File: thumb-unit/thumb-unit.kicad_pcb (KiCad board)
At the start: 2 copper layers, 82.5 x 79 mm, 24 parts, among them J1 Conn_01x10, SW1 SW_SPDT, SW2 SW_Push, SW3 SW_Push, SW4 SW_Push, SW5 SW_Push, U1 xiao-ble, U2 PMW3610, U3 TLV70218_SOT23-5

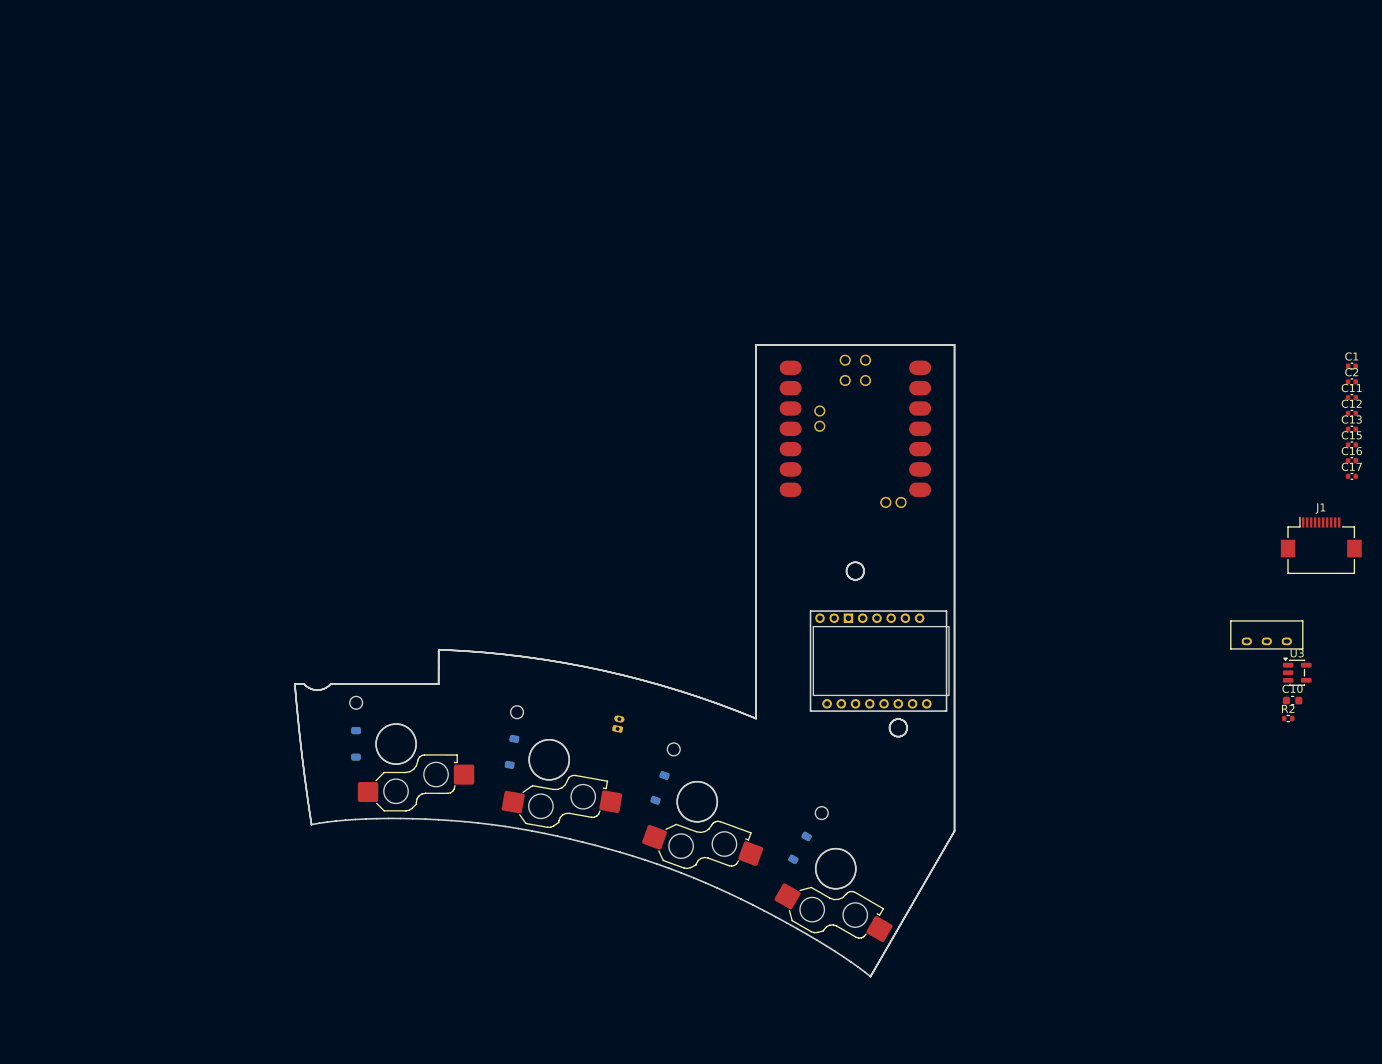
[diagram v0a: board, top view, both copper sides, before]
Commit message: feat: 親指ユニットのpcb設計
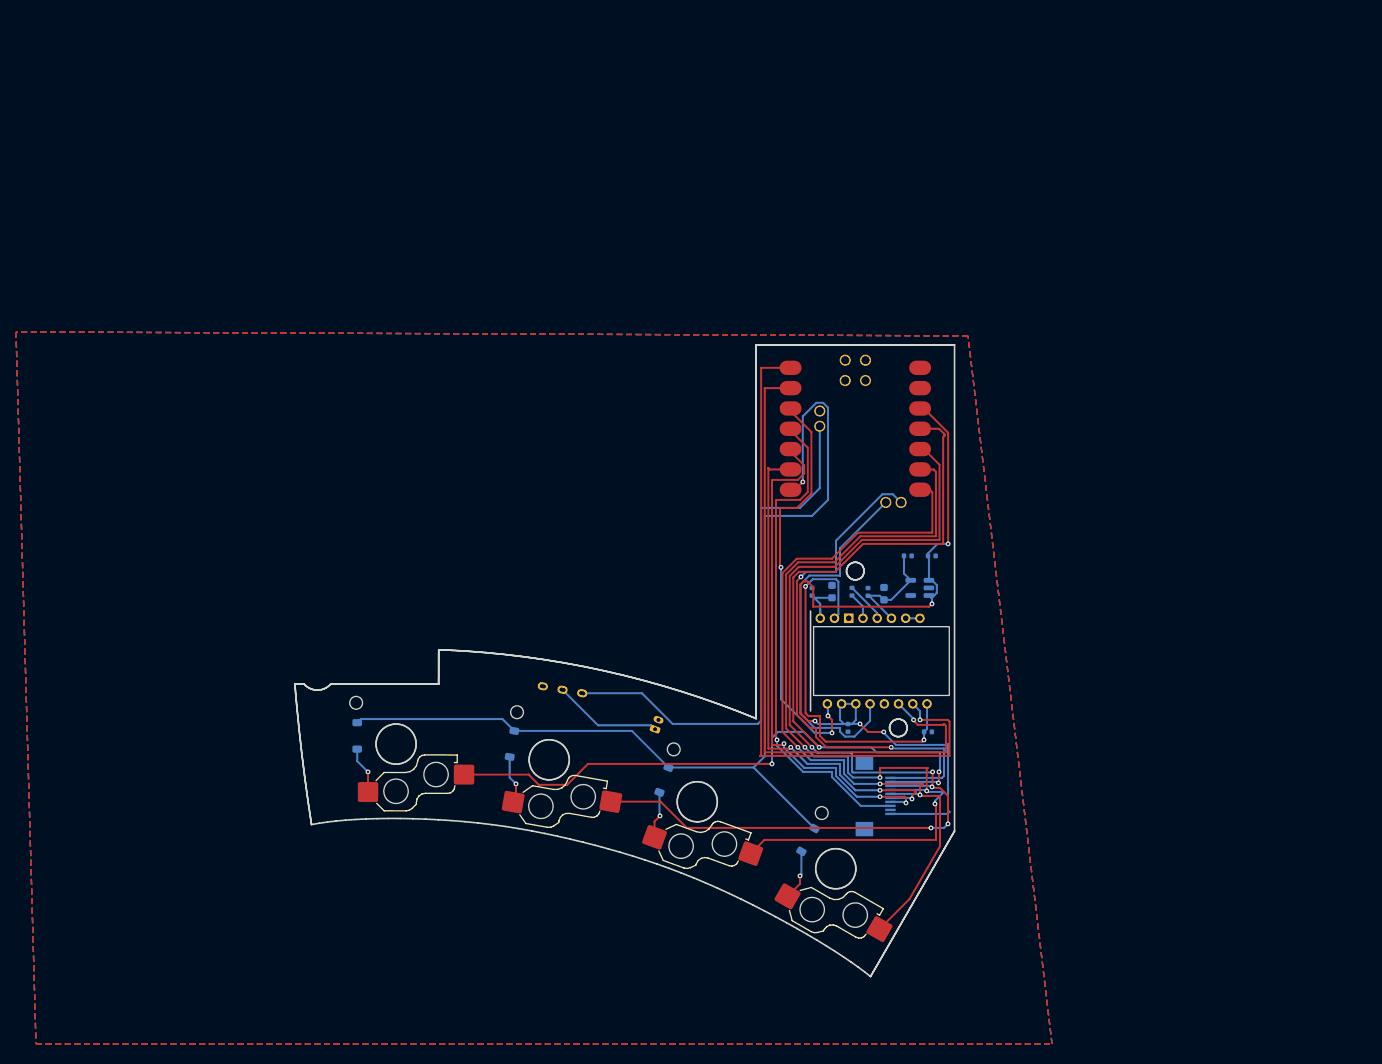
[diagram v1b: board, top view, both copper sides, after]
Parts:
- removed R2: 10k, Resistor_SMD:R_0402_1005Metric
- C1, C12, C15, C16, C2, J1, SW1, U3: moved to B.Cu
- C10: value 10uF -> 10uF X7R; moved to B.Cu
- C11: value 10nF -> 10nF X7R; moved to B.Cu
- C13: value 100nF -> 100nF X7R; moved to B.Cu
- C17: value 3.3uF -> 3.3uF/16V; footprint Capacitor_SMD:C_0402_1005Metric -> Capacitor_SMD:C_0603_1608Metric; moved to B.Cu
- moved SW1 88.1 mm to (106.0, 141.7), turned to 170 degrees
- moved C15 72.2 mm to (141.5, 147.5), turned to 90 degrees
- moved C11 71.7 mm to (137.0, 130.5), turned to -90 degrees
- moved C12 66.3 mm to (151.5, 148.0)
- moved C13 65.7 mm to (142.0, 130.5), turned to -90 degrees
- moved J1 64.4 mm to (144.9, 156.0), turned to 90 degrees
- moved C16 62.7 mm to (144.0, 130.5), turned to 90 degrees
- moved C17 60.3 mm to (146.0, 130.7), turned to 90 degrees
- moved C2 59.6 mm to (149.0, 126.0), turned to 180 degrees
- moved C10 59.2 mm to (139.5, 130.5), turned to -90 degrees
- moved C1 57.6 mm to (152.0, 126.0), turned to 180 degrees
- moved U3 48.3 mm to (150.5, 130.0), turned to 180 degrees
- moved BT1 4.68 mm to (117.4, 147.7), turned to 70 degrees
- moved D1 1.41 mm to (136.5, 161.5), turned to 60 degrees
- moved D2 1.12 mm to (118.5, 154.0), turned to 70 degrees
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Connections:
- C10 pad 1: Net-(U2-VCP) -> GND
- C10 pad 2: GND -> Net-(U2-VCP)
- C11 pad 1: Net-(U2-VCP) -> GND
- C11 pad 2: GND -> Net-(U2-VCP)
- C12 pad 1: +1V8 -> Net-(U2-+VCSEL)
- C12 pad 2: +1V8 -> GND
- C16 pad 1: GND -> +1V8
- C16 pad 2: +1V8 -> GND
- C17 pad 1: GND -> +1V8
- C17 pad 2: +1V8 -> GND
- U2 pad 1: +1V8 -> Net-(U2-+VCSEL)
- U2 pad 10: +1V8 -> Net-(U2-+VCSEL)
- U2 pad 15: +1V8 -> Net-(U2--VCSEL)
- U2 pad 16: +1V8 -> Net-(U2--VCSEL)
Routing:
- net /COL3: track 0.00 -> 135.4 mm, vias 0 -> 4
- net /COL2: track 0.00 -> 130.1 mm, vias 0 -> 5
- net /ROW3: track 0.00 -> 130.0 mm, vias 0 -> 1
- net /COL1: track 0.00 -> 112.4 mm, vias 0 -> 4
- net +3V3: track 0.00 -> 109.3 mm, vias 0 -> 5
- net /COL0: track 0.00 -> 95.3 mm, vias 0 -> 3
- net /SDIO: track 0.00 -> 85.9 mm, vias 0 -> 1
- net /SCLK: track 0.00 -> 81.6 mm, vias 0 -> 1
- net /COL4: track 0.00 -> 68.0 mm, vias 0 -> 2
- net /BAT_SW: track 0.00 -> 66.8 mm
- net /ROW1: track 0.00 -> 64.7 mm, vias 0 -> 3
- net /ROW2: track 0.00 -> 63.0 mm, vias 0 -> 3
- net /ROW0: track 0.00 -> 62.0 mm, vias 0 -> 1
- net /MOTION: track 0.00 -> 52.6 mm, vias 0 -> 3
- net Net-(U2-+VCSEL): track 0.00 -> 47.8 mm, vias 0 -> 2
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- added copper zone on B.Cu, net GND
- added copper zone on F.Cu, net GND
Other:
- outline, holes or cut-outs redrawn

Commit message: feat: 親指ユニットのpcb設計
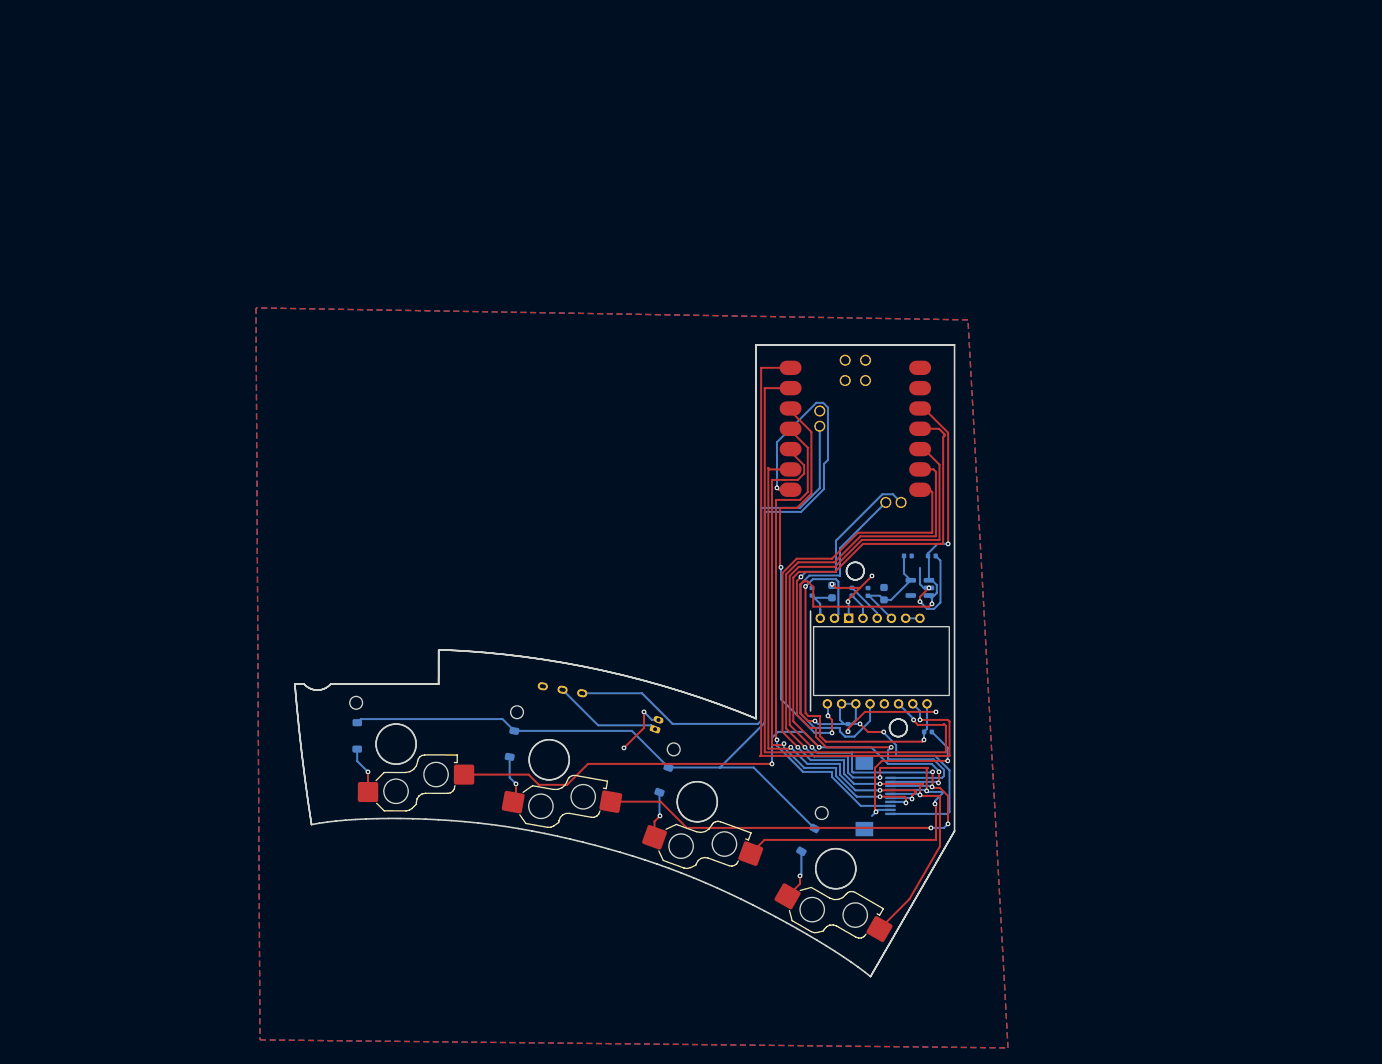
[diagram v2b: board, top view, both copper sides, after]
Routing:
- net GND: track 0.00 -> 67.4 mm, vias 0 -> 11
- net /ROW3: track 130.0 -> 132.0 mm
- net /COL3: track 135.4 -> 134.0 mm
- net +3V3: track 109.3 -> 108.1 mm

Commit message: feat: 親指dxfファイルをインポートして調整した
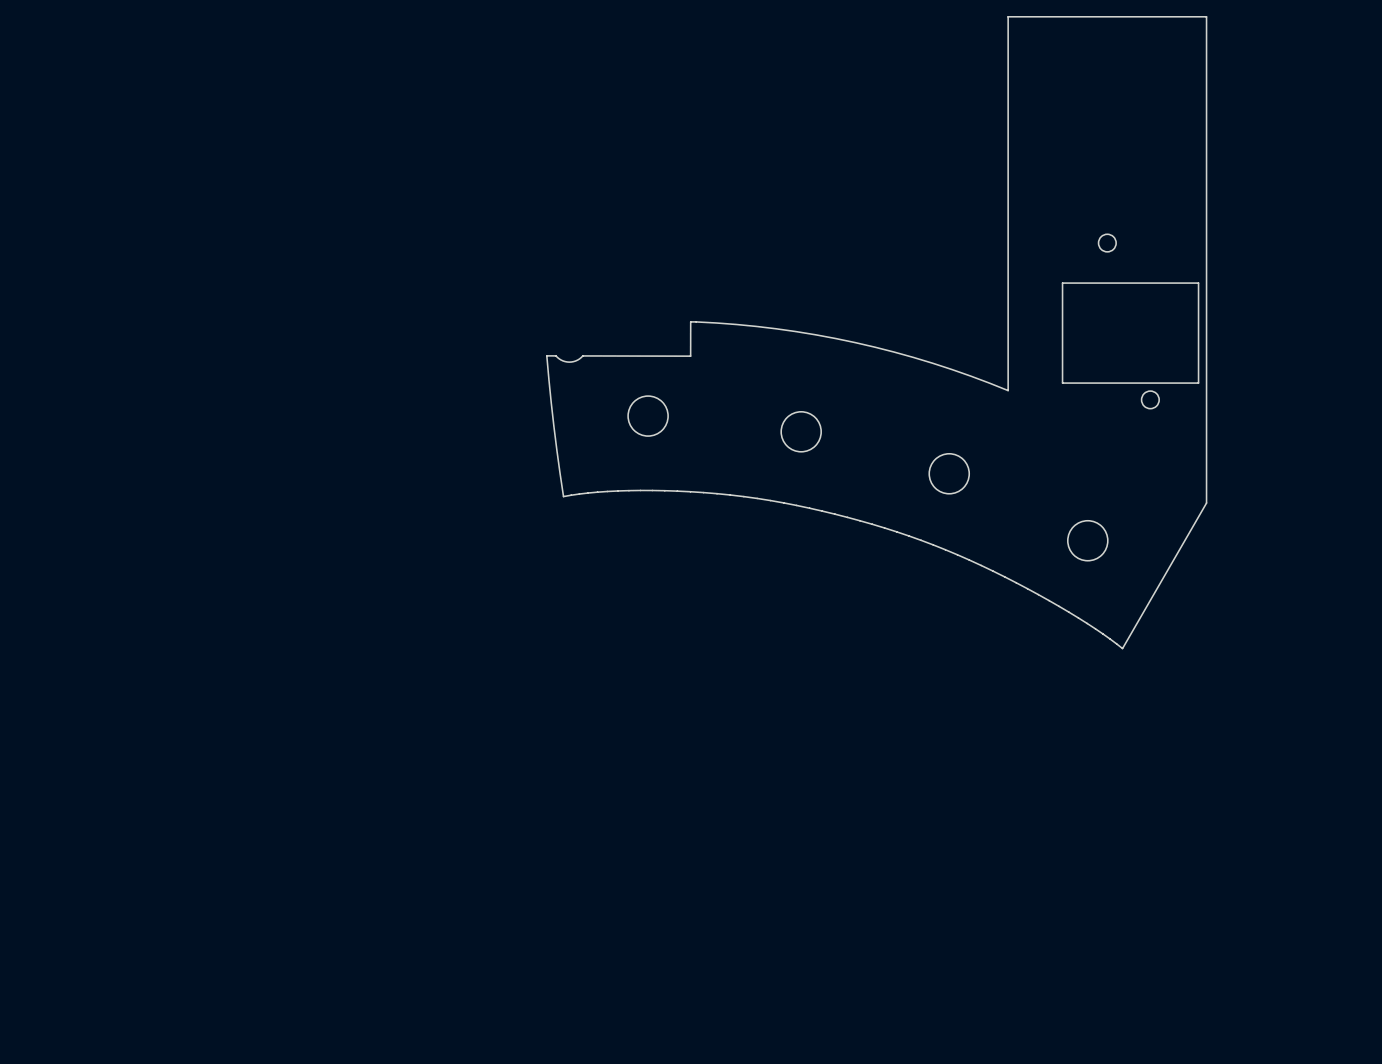
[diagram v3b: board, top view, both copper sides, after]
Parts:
- removed BT1: Battery, Connector_Molex:Molex_PicoBlade_53048-0210_1x02_P1.25mm_Horizontal
- removed C1: 1uF, Capacitor_SMD:C_0402_1005Metric
- removed C10: 10uF X7R, Capacitor_SMD:C_0603_1608Metric
- removed C11: 10nF X7R, Capacitor_SMD:C_0402_1005Metric
- removed C12: 10nF, Capacitor_SMD:C_0402_1005Metric
- removed C13: 100nF X7R, Capacitor_SMD:C_0402_1005Metric
- removed C15, C16: 100nF, Capacitor_SMD:C_0402_1005Metric
- removed C17: 3.3uF/16V, Capacitor_SMD:C_0603_1608Metric
- removed C2: 1uf, Capacitor_SMD:C_0402_1005Metric
- removed D1, D2, D3, D4: D, Diode_SMD:D_SOD-123
- removed J1: Conn_01x10, Connector_FFC-FPC:Hirose_FH12-10S-0.5SH_1x10-1MP_P0.50mm_Horizontal
- removed SW1: SW_SPDT, custom:TGSW_MSK-12D19
- removed SW2, SW3, SW4, SW5: SW_Push, PCM_Switch_Keyboard_Hotswap_Kailh:SW_Hotswap_Kailh_Choc_V2_1.00u
- removed U1: xiao-ble, mcu:xiao-ble-smd
- removed U2: PMW3610, sensor:PMW3610
- removed U3: TLV70218_SOT23-5, Package_TO_SOT_SMD:SOT-23-5
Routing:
- net /COL3: track 134.0 -> 0.00 mm, vias 4 -> 0
- net /ROW3: track 132.0 -> 0.00 mm, vias 1 -> 0
- net /COL2: track 130.1 -> 0.00 mm, vias 5 -> 0
- net /COL1: track 112.4 -> 0.00 mm, vias 4 -> 0
- net +3V3: track 108.1 -> 0.00 mm, vias 5 -> 0
- net /COL0: track 95.3 -> 0.00 mm, vias 3 -> 0
- net /SDIO: track 85.9 -> 0.00 mm, vias 1 -> 0
- net /SCLK: track 81.6 -> 0.00 mm, vias 1 -> 0
- net /COL4: track 67.8 -> 0.00 mm, vias 2 -> 0
- net GND: track 67.4 -> 0.00 mm, vias 11 -> 0
- net /BAT_SW: track 66.8 -> 0.00 mm
- net /ROW1: track 64.7 -> 0.00 mm, vias 3 -> 0
- net /ROW2: track 63.0 -> 0.00 mm, vias 3 -> 0
- net /ROW0: track 62.0 -> 0.00 mm, vias 1 -> 0
- net /MOTION: track 52.6 -> 0.00 mm, vias 3 -> 0
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- removed copper zone on B.Cu, net GND
- removed copper zone on F.Cu, net GND
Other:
- outline, holes or cut-outs redrawn

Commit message: feat: 親指ユニット・一旦完成
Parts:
- added BT1: Battery, Connector_Molex:Molex_PicoBlade_53048-0210_1x02_P1.25mm_Horizontal, B.Cu at (134.6, 106.3)
- added C1: 1uF, Capacitor_SMD:C_0402_1005Metric, B.Cu at (168.0, 112.0)
- added C10: 10uF X7R, Capacitor_SMD:C_0603_1608Metric, B.Cu at (173.5, 108.5)
- added C11: 10nF X7R, Capacitor_SMD:C_0402_1005Metric, B.Cu at (172.0, 108.0)
- added C12: 10nF, Capacitor_SMD:C_0402_1005Metric, B.Cu at (158.5, 92.0)
- added C13: 100nF X7R, Capacitor_SMD:C_0402_1005Metric, B.Cu at (165.5, 107.5)
- added C15: 100nF, Capacitor_SMD:C_0402_1005Metric, B.Cu at (169.0, 88.5)
- added C16: 100nF, Capacitor_SMD:C_0402_1005Metric, B.Cu at (165.0, 110.0)
- added C17: 3.3uF/16V, Capacitor_SMD:C_0603_1608Metric, B.Cu at (162.5, 107.0)
- added C2: 1uf, Capacitor_SMD:C_0402_1005Metric, B.Cu at (170.0, 112.0)
- added D1: D, Diode_SMD:D_SOD-123, B.Cu at (165.0, 127.5)
- added D2: D, Diode_SMD:D_SOD-123, B.Cu at (147.5, 118.0)
- added D3: D, Diode_SMD:D_SOD-123, B.Cu at (129.5, 112.0)
- added D4: D, Diode_SMD:D_SOD-123, B.Cu at (110.0, 109.2)
- added J1: Conn_01x10, Connector_FFC-FPC:Hirose_FH12-10S-0.5SH_1x10-1MP_P0.50mm_Horizontal, B.Cu at (164.4, 117.0)
- added SW1: SW_SPDT, custom:TGSW_MSK-12D19, B.Cu at (125.5, 102.0)
- added SW2: SW_Push, PCM_Switch_Keyboard_Hotswap_Kailh:SW_Hotswap_Kailh_Choc_V2_1.00u, F.Cu at (160.0, 125.6)
- added SW3: SW_Push, PCM_Switch_Keyboard_Hotswap_Kailh:SW_Hotswap_Kailh_Choc_V2_1.00u, F.Cu at (142.7, 117.2)
- added SW4: SW_Push, PCM_Switch_Keyboard_Hotswap_Kailh:SW_Hotswap_Kailh_Choc_V2_1.00u, F.Cu at (124.1, 112.0)
- added SW5: SW_Push, PCM_Switch_Keyboard_Hotswap_Kailh:SW_Hotswap_Kailh_Choc_V2_1.00u, F.Cu at (105.0, 110.2)
- added U1: xiao-ble, mcu:xiao-ble-smd, F.Cu at (162.4, 70.6)
- added U2: PMW3610, sensor:PMW3610, B.Cu at (164.3, 99.6)
- added U3: TLV70218_SOT23-5, Package_TO_SOT_SMD:SOT-23-5, B.Cu at (172.1, 115.5)
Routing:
- net /COL3: track 0.00 -> 146.8 mm, vias 0 -> 3
- net /COL2: track 0.00 -> 132.9 mm, vias 0 -> 3
- net +3V3: track 0.00 -> 119.8 mm, vias 0 -> 3
- net /COL1: track 0.00 -> 112.4 mm, vias 0 -> 3
- net /ROW3: track 0.00 -> 109.8 mm, vias 0 -> 1
- net /COL0: track 0.00 -> 100.6 mm, vias 0 -> 3
- net /BAT_SW: track 0.00 -> 65.4 mm, vias 0 -> 2
- net GND: track 0.00 -> 62.0 mm, vias 0 -> 11
- net /ROW0: track 0.00 -> 60.1 mm, vias 0 -> 1
- net /COL4: track 0.00 -> 56.7 mm
- net /ROW1: track 0.00 -> 56.2 mm, vias 0 -> 1
- net /ROW2: track 0.00 -> 51.7 mm, vias 0 -> 1
- net /SDIO: track 0.00 -> 39.6 mm, vias 0 -> 1
- net /MOTION: track 0.00 -> 38.3 mm, vias 0 -> 1
- net /SCLK: track 0.00 -> 36.4 mm, vias 0 -> 1
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- added copper zone on B.Cu, net GND
- added copper zone on F.Cu, net GND
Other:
- outline, holes or cut-outs redrawn

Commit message: feat: 回路図完成
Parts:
- added R1: 10k, Resistor_SMD:R_0603_1608Metric, B.Cu at (182.5, 107.5)
- BT1: footprint Connector_Molex:Molex_PicoBlade_53048-0210_1x02_P1.25mm_Horizontal -> Connector_Molex:Molex_PicoBlade_53261-0271_1x02-1MP_P1.25mm_Horizontal
- U1: footprint mcu:xiao-ble-smd -> mcu:xiao-ble-tht
- moved C1 25.4 mm to (186.0, 130.0), turned to 180 degrees
- moved BT1 24.9 mm to (150.5, 125.5)
- moved C13 24.7 mm to (183.0, 125.0)
- moved C17 23.4 mm to (178.0, 124.5), turned to -90 degrees
- moved C15 22.0 mm to (180.0, 107.5)
- moved U3 21.6 mm to (184.0, 133.5)
- moved C12 21.6 mm to (173.0, 108.0)
- moved C2 21.4 mm to (181.5, 130.0), turned to 0 degrees
- moved SW1 21.0 mm to (138.6, 118.4)
- moved U1 21.0 mm to (175.4, 87.1)
- moved U2 21.0 mm to (177.3, 116.1)
- moved C10 21.0 mm to (186.5, 125.0)
- moved C11 21.0 mm to (185.0, 124.5)
- moved SW2 21.0 mm to (173.0, 142.1)
- moved SW3 21.0 mm to (155.7, 133.7)
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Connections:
- U2 pad 7: +3V3 -> Net-(U2-~{RESET})
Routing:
- net GND: track 62.0 -> 105.7 mm, vias 11 -> 9
- net /COL0: track 100.6 -> 72.0 mm
- net +3V3: track 119.8 -> 95.2 mm, vias 3 -> 2
- net /BAT_SW: track 65.4 -> 80.6 mm, vias 2 -> 0
- net /COL1: track 112.4 -> 97.9 mm, vias 3 -> 2
- net +1V8: track 22.5 -> 14.9 mm, vias 0 -> 3
- net /MOTION: track 38.3 -> 45.2 mm
- net Net-(U2-+VCSEL): track 31.9 -> 38.5 mm
- net /COL3: track 146.8 -> 152.7 mm, vias 3 -> 2
- net /COL2: track 132.9 -> 128.8 mm
- net Net-(U2-~{RESET}): track 0.00 -> 2.98 mm, vias 0 -> 1
- net /SDIO: track 39.6 -> 37.0 mm, vias 1 -> 2
- net Net-(U2-C-): track 3.02 -> 5.58 mm, vias 0 -> 1
- net /SCLK: track 36.4 -> 34.7 mm
- net /COL4: track 56.7 -> 58.3 mm
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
